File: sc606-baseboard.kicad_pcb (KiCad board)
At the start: 2 copper layers, 100 x 76 mm, 391 parts, among them IC1 TPS54561DPRT, IC2 TPS7A0518PDBVT, J1 PJ-202A, J10 WE_632723300011, J11 WE_632723300011, J2 WE_68715014522, J3 F52R-1A7H1-11020, J4 46756-1001, J5 U_FL-R-SMT-1_10_, J6 U_FL-R-SMT-1_10_, J7 DM3AT-SF-PEJM5, J8 693022010811, J9 0473460001, M1 SC606T, Q1 BSS138APW, Q2 BSS138-7-F, Q3 BSS138APW, Q4 BSS138APW, Q5 BSS138APW, Q6 BSS138APW, Q7 BSS138-7-F, Q8 BSS138-7-F, SW1 1X03, U1 AP62301WU-7, U10 NCP163ASN330T1G, U11 EMIF06-MSD02N16, U12 FSUSB30MUX, U13 FT232RQ-REEL, U14 GSB3112311HR, U15 USB57442G, U2 AP62301WU-7, U3 AP62301WU-7, U4 74LVC1G123GN, U5 NTS0102GT, U6 PCA9547BS, U7 LT9611UXC, U8 NTS0102GT, U9 TPD13S523PWR, Y1 ABM8G-24.000MHZ-18-D2Y-T, Y2 ABM8G-25.000MHZ-B4Y-T

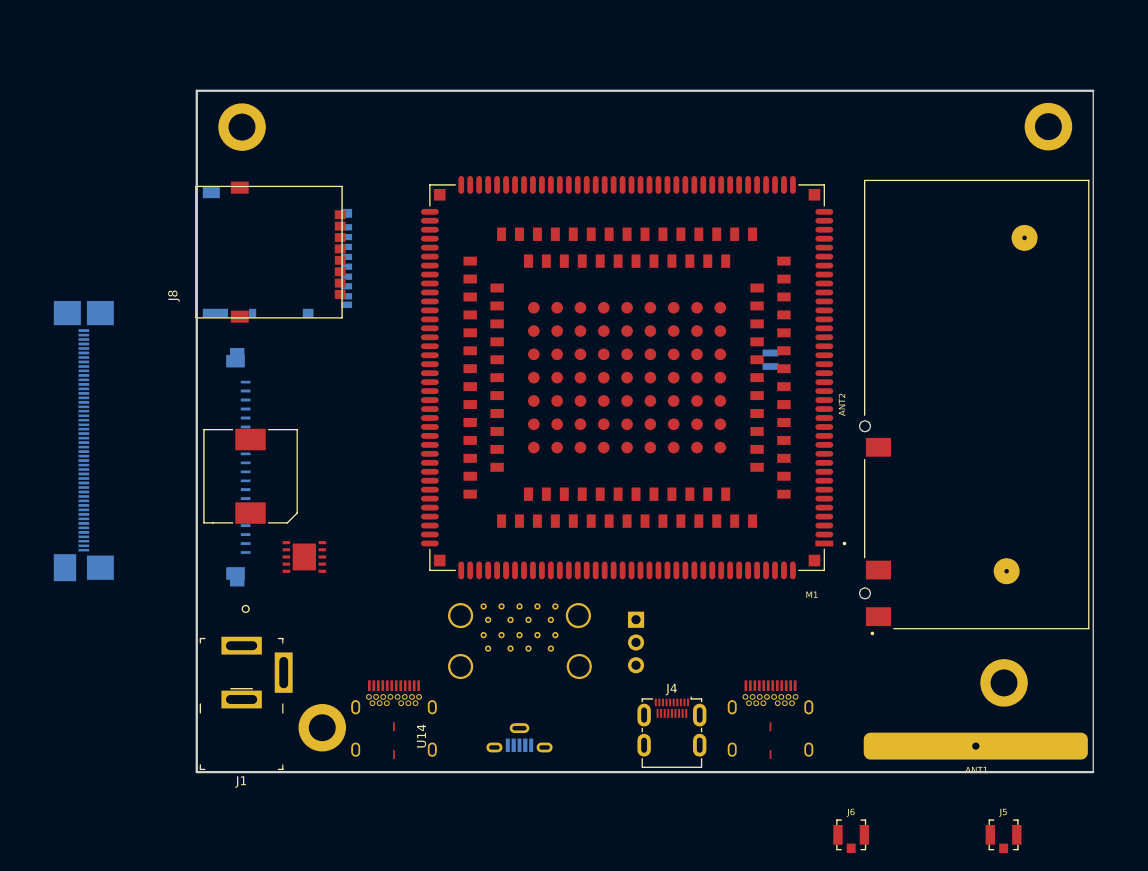
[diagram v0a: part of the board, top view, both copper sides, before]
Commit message: Adding missing 3D models of components
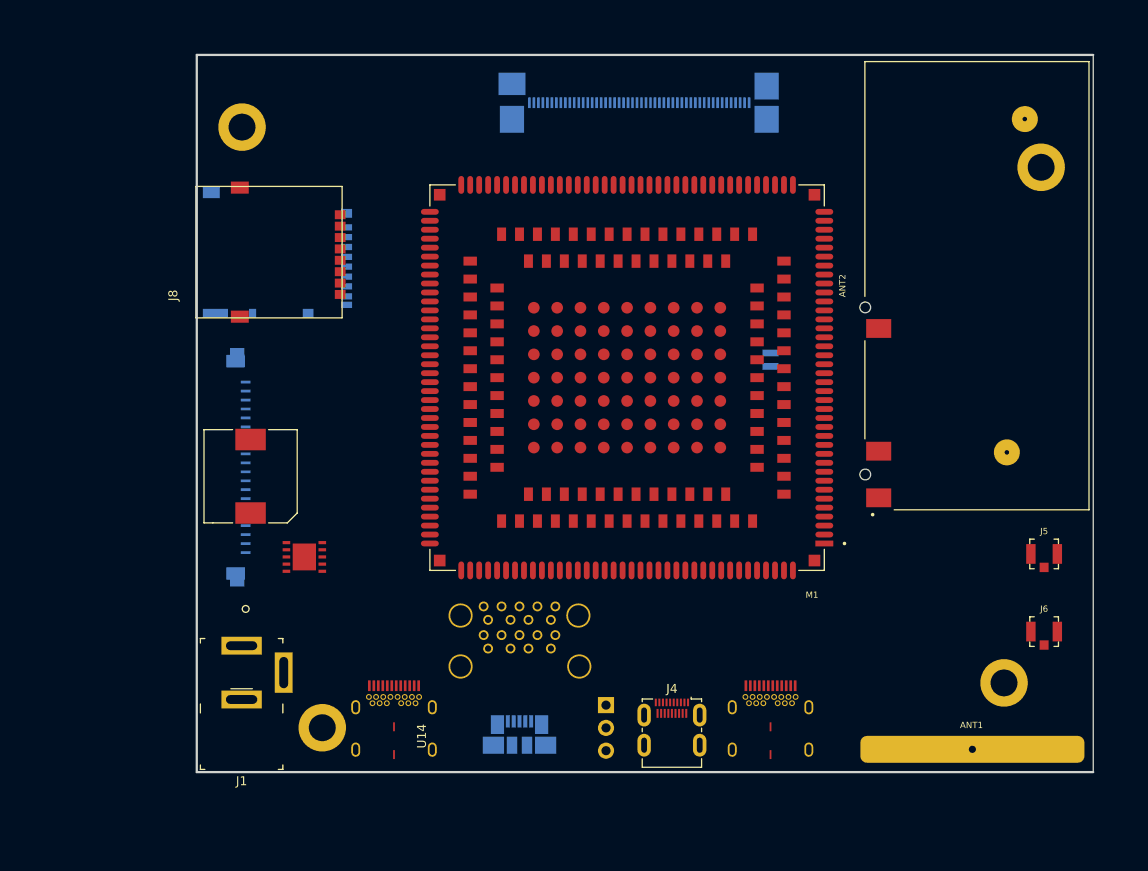
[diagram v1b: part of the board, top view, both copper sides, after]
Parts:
- J9: footprint sc606-baseboard-footprints:USB_Micro_B_Female_Vert_1051330001 -> sc606-baseboard-footprints:USB_Micro_B_Female_0473460001
- moved J2 71.7 mm to (124.4, 55.9), turned to 0 degrees
- moved J5 31.7 mm to (169.5, 105.7)
- moved J6 31.3 mm to (169.5, 114.3)
- moved ANT2 13.3 mm to (162.0, 75.7)
- moved SW1 10.1 mm to (120.7, 122.5)
- moved MP4 4.61 mm to (169.1, 62.5)
- moved ANT1 0.81 mm to (161.4, 127.6), turned to 180 degrees
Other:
- board size 100 x 76 mm -> 100 x 80 mm

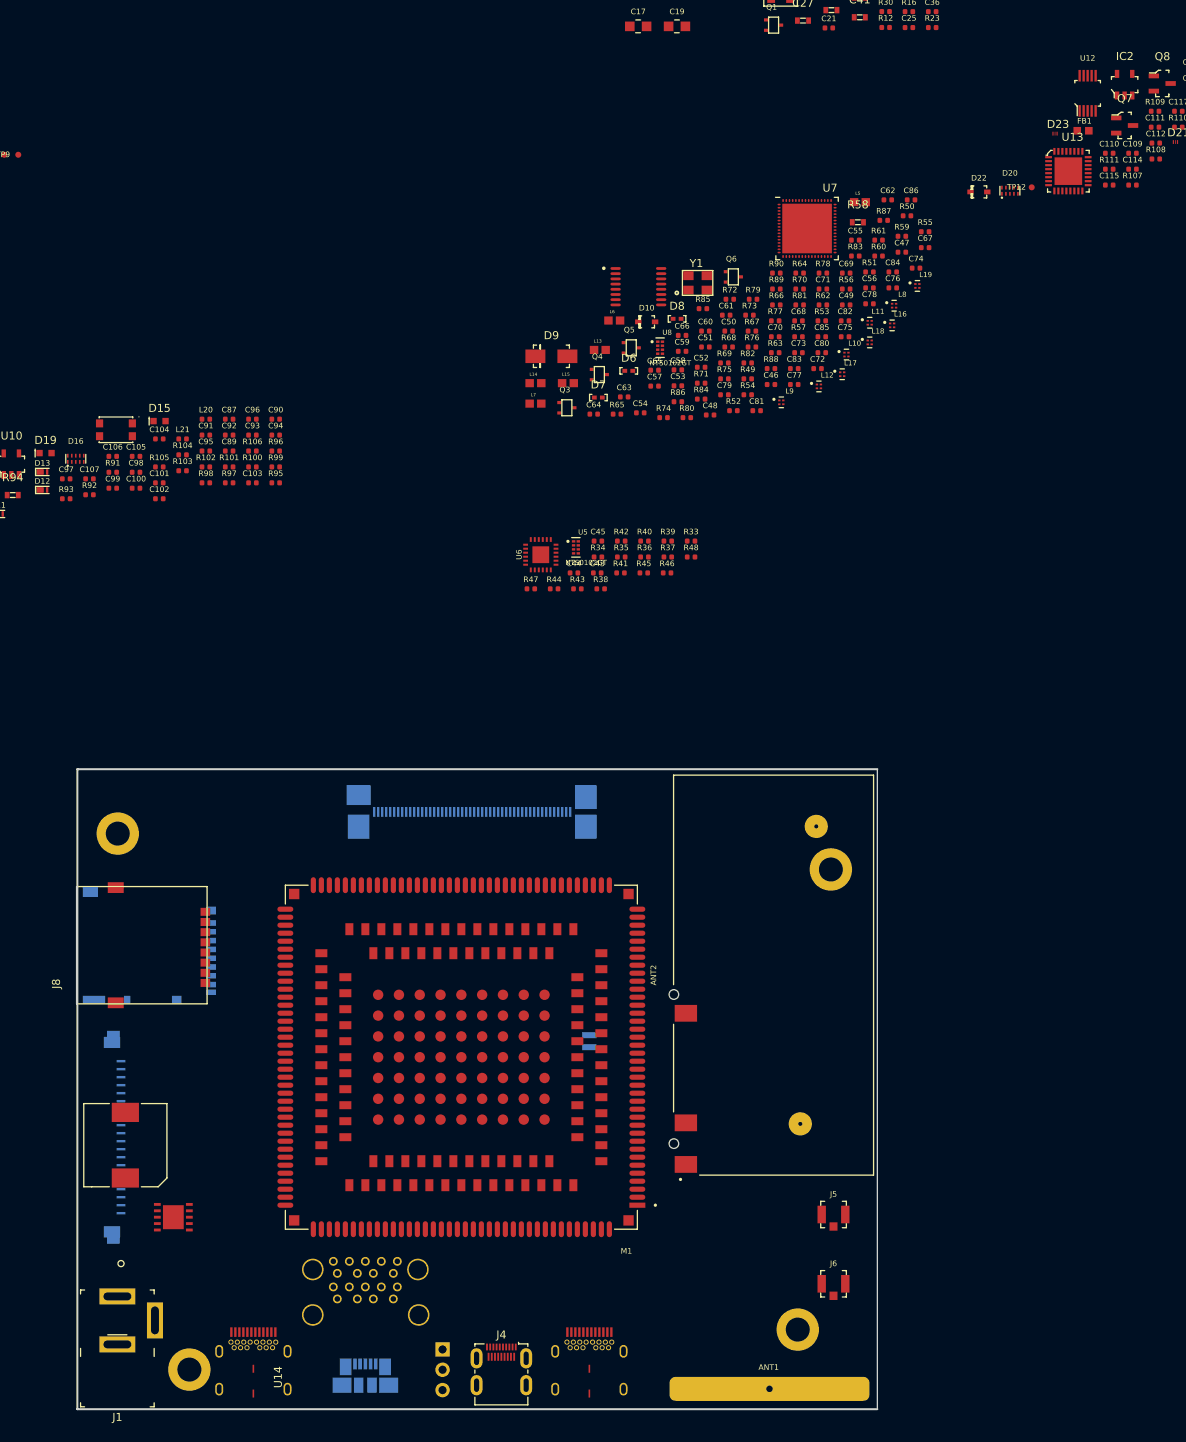
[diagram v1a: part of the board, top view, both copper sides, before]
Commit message: Added USB A and C double stack connector
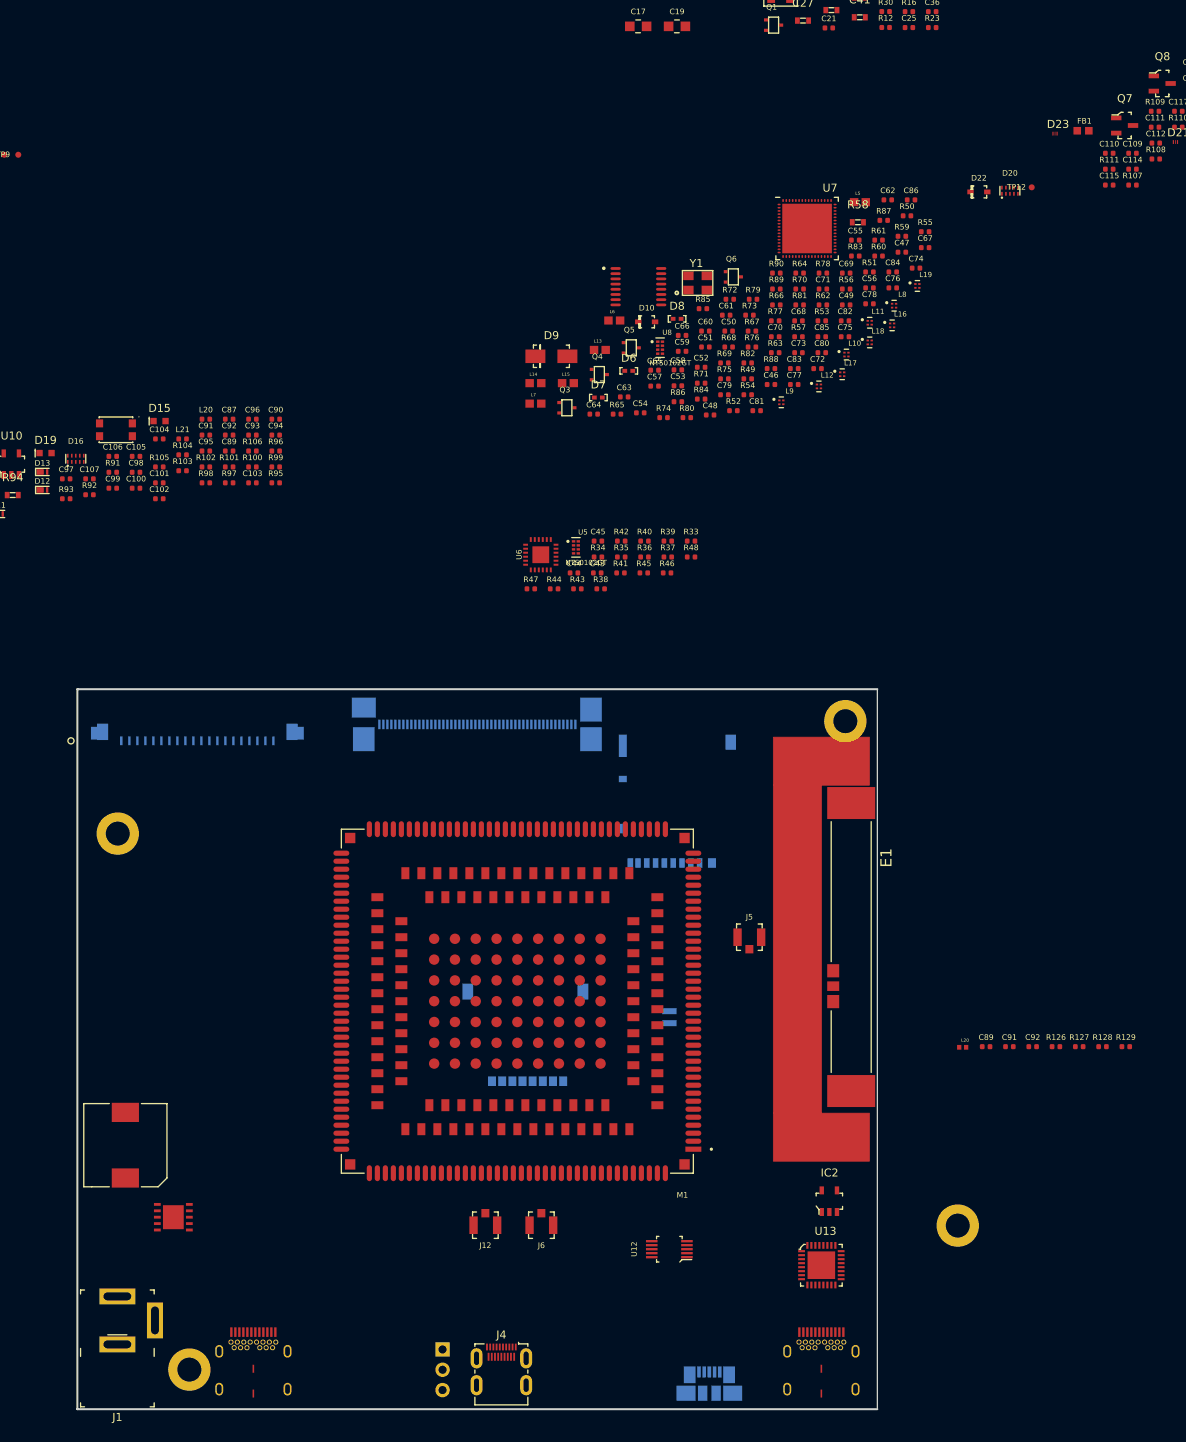
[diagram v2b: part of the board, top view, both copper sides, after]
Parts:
- removed ANT1: GPS-ANT050-external-antenna, sc606-baseboard-footprints:GPS-ANT050-mounting-pad
- removed ANT2: PRO-OB-572_DCPOL, sc606-baseboard-footprints:PRO-OB-572_2
- removed U14: GSB3112311HR, sc606-baseboard-footprints:GSB3112311HR
- added C89: C_1u_0402, sc606-baseboard-footprints:0402-cap, F.Cu at (188.6, 84.7)
- added C91: C_1u_0402, sc606-baseboard-footprints:0402-cap, F.Cu at (191.5, 84.7)
- added C92: C_3p_0402, sc606-baseboard-footprints:0402-cap, F.Cu at (194.4, 84.7)
- added E1: ANT-LTE-CER-T, sc606-baseboard-footprints:XDCR_ANT-LTE-CER-T, F.Cu at (171.7, 72.2)
- added J12: U_FL-R-SMT-1_10_, sc606-baseboard-footprints:Coax_Conn_U.FL, F.Cu at (126.0, 107.0)
- added L20: HK10056N8S-T, sc606-baseboard-footprints:INDC1005X55N, F.Cu at (185.7, 84.8)
- added R126: R_0R_0402, sc606-baseboard-footprints:0402-res, F.Cu at (197.3, 84.7)
- added R127: R_0R_0402, sc606-baseboard-footprints:0402-res, F.Cu at (200.2, 84.7)
- added R128: R_0R_0402, sc606-baseboard-footprints:0402-res, F.Cu at (203.1, 84.7)
- added R129: R_0R_0402, sc606-baseboard-footprints:0402-res, F.Cu at (206.1, 84.7)
- J8: moved to B.Cu
- moved U12 153.7 mm to (149.0, 110.0), turned to 90 degrees
- moved IC2 144.4 mm to (169.0, 104.0)
- moved U13 140.2 mm to (168.5, 112.5)
- moved J7 68.4 mm to (150.0, 54.0), turned to 0 degrees
- moved J3 53.4 mm to (90.0, 44.0), turned to 0 degrees
- moved J8 43.5 mm to (131.0, 89.0), turned to 180 degrees
- moved J9 43.0 mm to (154.0, 128.0)
- moved J6 37.2 mm to (133.0, 107.0), turned to 180 degrees
- moved J5 36.2 mm to (159.0, 71.0)
- moved J10 29.0 mm to (168.0, 126.0)
- moved MP3 23.9 mm to (185.0, 107.0)
- moved MP4 18.6 mm to (170.9, 44.0)
- moved J2 10.9 mm to (125.0, 45.0)
- moved BAT1 10.4 mm to (149.0, 81.0)
- moved M1 9.90 mm to (130.0, 79.0)
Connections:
- M1 pad 129: Net-(M1-Pad129) -> ANT-WIFI
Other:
- board size 100 x 80 mm -> 100 x 90 mm
